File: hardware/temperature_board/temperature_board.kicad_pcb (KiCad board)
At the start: 2 copper layers, 95 x 20 mm, 13 parts, among them J1 RJ45, U1 TSIC50XF, U2 ST485, m3_loch VAL**

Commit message: checking
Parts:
- removed the m3_loch at (230.0, 150.0)
- removed the m3_loch at (200.0, 140.0)
- added m3_loch: VAL**, m3_loch, F.Cu at (134.0, 102.0)
- added m3_loch: VAL**, m3_loch, F.Cu at (104.0, 92.0)
- moved C1 107.3 mm to (106.0, 102.0)
- moved C2 107.3 mm to (115.0, 102.0)
- moved C3 107.3 mm to (115.0, 92.0)
- moved C4 107.3 mm to (125.0, 99.0)
- moved J1 107.3 mm to (144.5, 97.0)
- moved R1 107.3 mm to (110.0, 102.0)
- moved R2 107.3 mm to (122.0, 101.0)
- moved R3 107.3 mm to (122.0, 93.0)
- moved R4 107.3 mm to (125.0, 95.0)
- moved U1 107.3 mm to (73.0, 97.0)
- moved U2 107.3 mm to (117.0, 97.0)
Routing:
- net GND: track 142.1 -> 143.1 mm
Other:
- net class uc added: clearance 0.254, trace_width 0.4, via_dia 1.2, via_drill 0.6

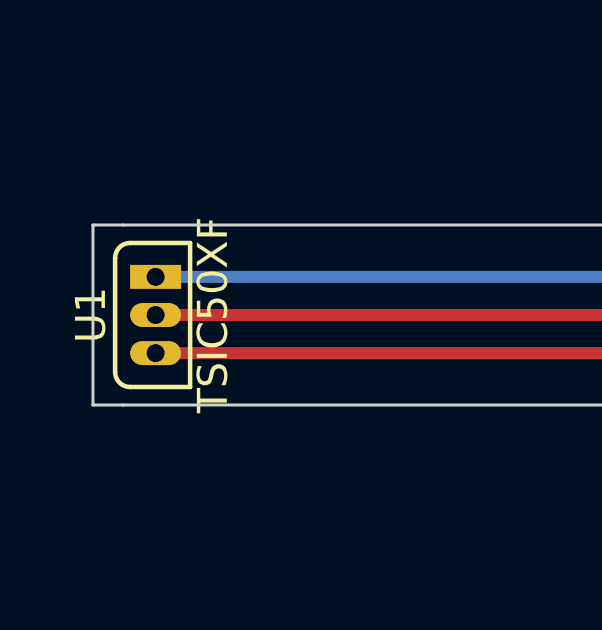
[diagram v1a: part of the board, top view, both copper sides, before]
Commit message: change sensor modules
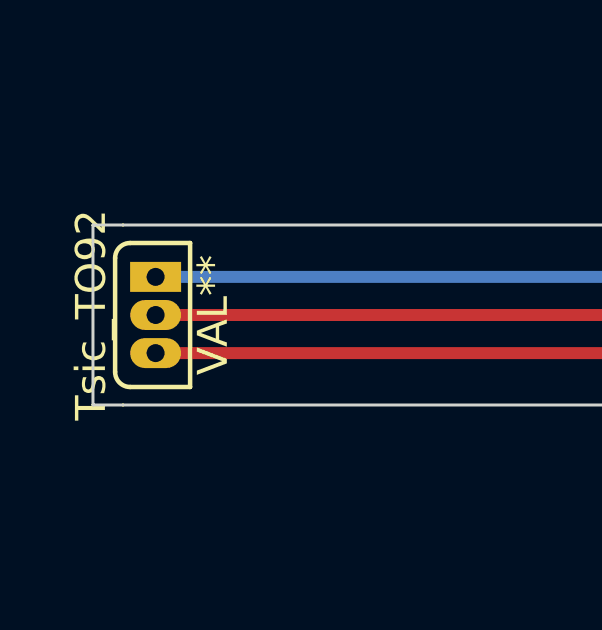
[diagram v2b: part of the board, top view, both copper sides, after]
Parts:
- removed U1: TSIC50XF, Tsic_TO92
- added Tsic_TO92: VAL**, Tsic_TO92, F.Cu at (73.0, 97.0)
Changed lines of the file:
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@@
 (kicad_pcb (version 3) (host pcbnew "(2013-may-18)-stable")
   (general
-    (links 27)
+    (links 24)
     (no_connects 0)
     (area 53.714288 80.150001 208.999999 118.7)
@@
     (add_net N-000007)
   )
+  (module Tsic_TO92 (layer F.Cu)
+    (at 73 97 270)
+    (fp_text reference Tsic_TO92 (at 0 4.064 270) (layer F.SilkS)
+      (effects (font (size 1 1) (thickness 0.15)))
+    )
+    (fp_text value VAL** (at 0 0 270) (layer F.SilkS)
+      (effects (font (size 1 1) (thickness 0.15)))
+    )
+    (fp_arc (start 1.9 2.762) (end 2.4 2.762) (angle 90) (layer F.SilkS) (width 0.15))
+    (fp_arc (start -1.9 2.762) (end -1.9 3.262) (angle 90) (layer F.SilkS) (width 0.15))
+    (fp_line (start -2.4 0.762) (end 2.4 0.762) (layer F.SilkS) (width 0.15))
+    (fp_line (start 2.4 0.762) (end 2.4 2.762) (layer F.SilkS) (width 0.15))
+    (fp_line (start 1.9 3.262) (end -1.9 3.262) (layer F.SilkS) (width 0.15))
+    (fp_line (start -2.4 2.762) (end -2.4 0.762) (layer F.SilkS) (width 0.15))
+    (pad 2 thru_hole oval (at 0 1.912 270) (size 1 1.7) (drill 0.6)
+      (layers *.Cu *.Mask F.SilkS)
+    )
+    (pad 1 thru_hole trapezoid (at -1.27 1.912 270) (size 1 1.7) (drill 0.6)
+      (layers *.Cu *.Mask F.SilkS)
+    )
+    (pad 3 thru_hole oval (at 1.27 1.912 270) (size 1 1.7) (drill 0.6)
+      (layers *.Cu *.Mask F.SilkS)
+    )
+  )
   (module RJ45_8P8_simple (layer F.Cu)
     (at 144.5 97 270)
@@
       (scale (xyz 0.4 0.4 0.4))
       (rotate (xyz 0 0 0))
-    )
-  )
-  (module Tsic_TO92 (layer F.Cu)
-    (at 73 97 270)
-    (fp_text reference U1 (at 0 4.064 270) (layer F.SilkS)
-      (effects (font (size 1 1) (thickness 0.15)))
-    )
-    (fp_text value TSIC50XF (at 0 0 270) (layer F.SilkS)
-      (effects (font (size 1 1) (thickness 0.15)))
-    )
-    (fp_arc (start 1.9 2.762) (end 2.4 2.762) (angle 90) (layer F.SilkS) (width 0.15))
-    (fp_arc (start -1.9 2.762) (end -1.9 3.262) (angle 90) (layer F.SilkS) (width 0.15))
-    (fp_line (start -2.4 0.762) (end 2.4 0.762) (layer F.SilkS) (width 0.15))
-    (fp_line (start 2.4 0.762) (end 2.4 2.762) (layer F.SilkS) (width 0.15))
-    (fp_line (start 1.9 3.262) (end -1.9 3.262) (layer F.SilkS) (width 0.15))
-    (fp_line (start -2.4 2.762) (end -2.4 0.762) (layer F.SilkS) (width 0.15))
-    (pad 2 thru_hole oval (at 0 1.912 270) (size 0.8 1.7) (drill 0.6)
-      (layers *.Cu *.Mask F.SilkS)
-      (net 6 N-000007)
-    )
-    (pad 1 thru_hole trapezoid (at -1.27 1.912 270) (size 0.8 1.7) (drill 0.6)
-      (layers *.Cu *.Mask F.SilkS)
-      (net 3 GND)
-    )
-    (pad 3 thru_hole oval (at 1.27 1.912 270) (size 0.8 1.7) (drill 0.6)
-      (layers *.Cu *.Mask F.SilkS)
-      (net 4 N-0000010)
     )
   )
@@
   (segment (start 125 94.055) (end 122.11 94.055) (width 0.7) (layer F.Cu) (net 2))
   (segment (start 122.11 94.055) (end 122 93.945) (width 0.7) (layer F.Cu) (net 2))
-  (segment (start 71.088 95.73) (end 99.73 95.73) (width 0.4) (layer B.Cu) (net 3))
+  (segment (start 71.088 95.73) (end 99.73 95.73) (width 0.4) (layer B.Cu) (net 3) (status 10))
   (segment (start 118.3 90.5) (end 119.8 92) (width 0.4) (layer B.Cu) (net 3))
   (segment (start 113.5 90.5) (end 118.3 90.5) (width 0.4) (layer B.Cu) (net 3))
@@
   (segment (start 117 102) (end 115.945 102) (width 0.7) (layer F.Cu) (net 3))
   (segment (start 118.2 100.8) (end 117 102) (width 0.7) (layer F.Cu) (net 3))
-  (segment (start 71.088 98.27) (end 98.27 98.27) (width 0.4) (layer F.Cu) (net 4))
+  (segment (start 71.088 98.27) (end 98.27 98.27) (width 0.4) (layer F.Cu) (net 4) (status 10))
   (segment (start 107.555 100.5) (end 109.055 102) (width 0.4) (layer F.Cu) (net 4))
   (segment (start 100.5 100.5) (end 107.555 100.5) (width 0.4) (layer F.Cu) (net 4))
@@
   (segment (start 106.945 102) (end 109.055 102) (width 0.7) (layer F.Cu) (net 4))
   (segment (start 125 95.945) (end 125 98.055) (width 0.7) (layer F.Cu) (net 5))
-  (segment (start 71.088 97) (end 99 97) (width 0.4) (layer F.Cu) (net 6))
+  (segment (start 71.088 97) (end 99 97) (width 0.4) (layer F.Cu) (net 6) (status 10))
   (segment (start 100.902 98.902) (end 111.9 98.902) (width 0.4) (layer F.Cu) (net 6))
   (segment (start 99 97) (end 100.902 98.902) (width 0.4) (layer F.Cu) (net 6))

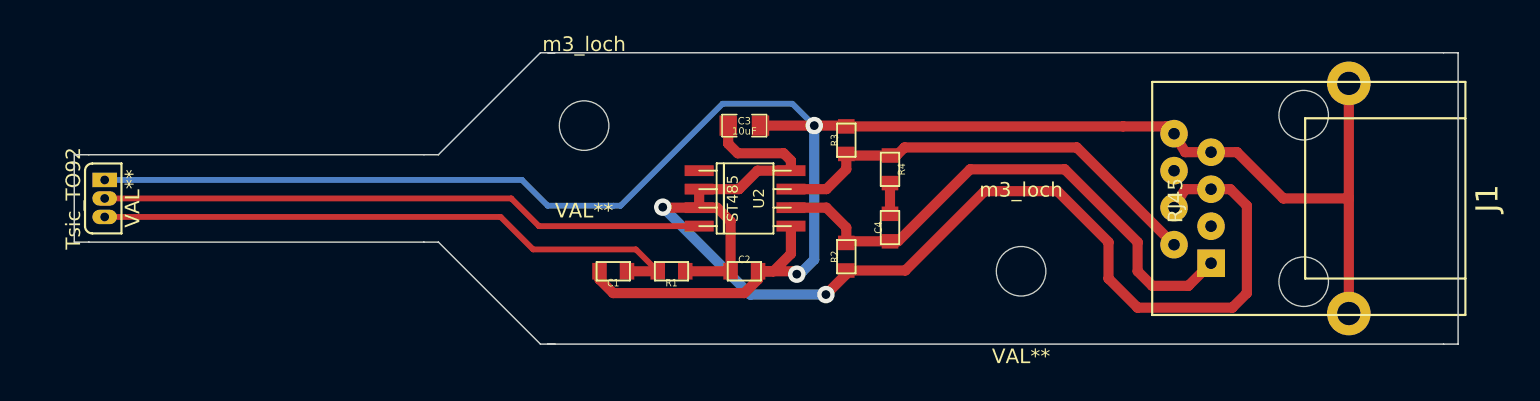
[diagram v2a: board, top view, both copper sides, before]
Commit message: change humidity
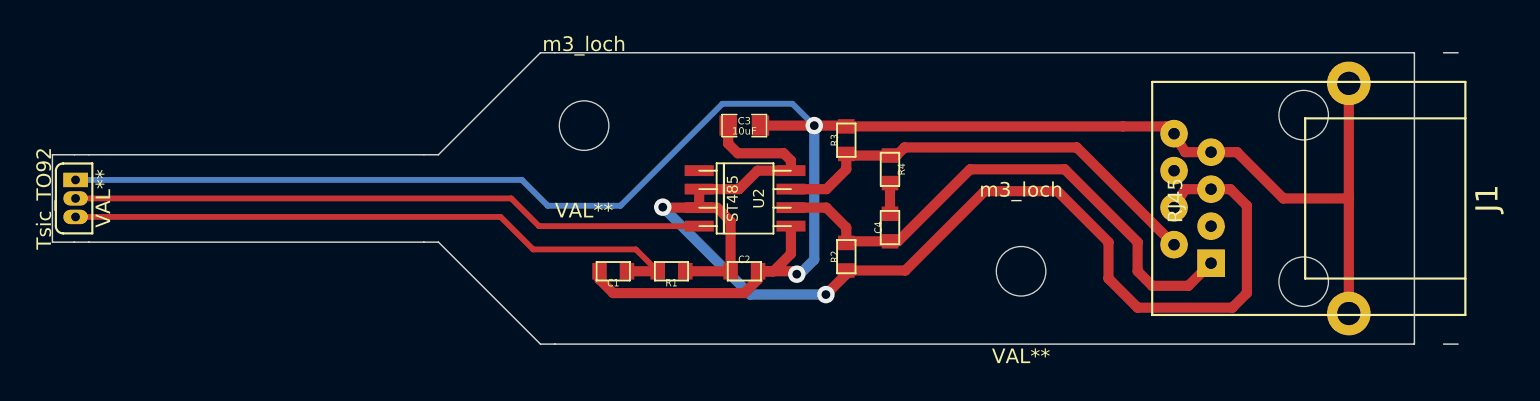
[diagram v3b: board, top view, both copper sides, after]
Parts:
- moved Tsic_TO92 2.00 mm to (71.0, 97.0)
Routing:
- net N-000007: track 41.6 -> 43.6 mm
- net N-0000010: track 41.6 -> 43.6 mm
- net GND: track 143.1 -> 145.1 mm
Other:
- board size 95 x 20 mm -> 96.5 x 20 mm
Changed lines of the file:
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@@
     (area 53.714288 80.150001 208.999999 118.7)
     (thickness 1.6)
-    (drawings 23)
+    (drawings 24)
     (tracks 102)
     (zones 0)
@@
   )
   (module Tsic_TO92 (layer F.Cu)
-    (at 73 97 270)
+    (at 71 97 270)
     (fp_text reference Tsic_TO92 (at 0 4.064 270) (layer F.SilkS)
       (effects (font (size 1 1) (thickness 0.15)))
@@
     )
   )
-  (dimension 27 (width 0.3) (layer Cmts.User)
-    (gr_text "27.000 mm" (at 131.5 111.349999) (layer Cmts.User)
+  (gr_line (start 67.5 100) (end 69 100) (angle 90) (layer Edge.Cuts) (width 0.1))
+  (gr_line (start 67.5 94) (end 67.5 100) (angle 90) (layer Edge.Cuts) (width 0.1))
+  (gr_line (start 69 94) (end 67.5 94) (angle 90) (layer Edge.Cuts) (width 0.1))
+  (dimension 92 (width 0.3) (layer Cmts.User)
+    (gr_text "92.000 mm" (at 115 116.849999) (layer Cmts.User)
       (effects (font (size 1.5 1.5) (thickness 0.3)))
     )
-    (feature1 (pts (xy 145 98) (xy 145 112.699999)))
-    (feature2 (pts (xy 118 98) (xy 118 112.699999)))
-    (crossbar (pts (xy 118 109.999999) (xy 145 109.999999)))
-    (arrow1a (pts (xy 145 109.999999) (xy 143.873497 110.586419)))
-    (arrow1b (pts (xy 145 109.999999) (xy 143.873497 109.413579)))
-    (arrow2a (pts (xy 118 109.999999) (xy 119.126503 110.586419)))
-    (arrow2b (pts (xy 118 109.999999) (xy 119.126503 109.413579)))
-  )
+    (feature1 (pts (xy 69 109) (xy 69 118.199999)))
+    (feature2 (pts (xy 161 109) (xy 161 118.199999)))
+    (crossbar (pts (xy 161 115.499999) (xy 69 115.499999)))
+    (arrow1a (pts (xy 69 115.499999) (xy 70.126503 114.913579)))
+    (arrow1b (pts (xy 69 115.499999) (xy 70.126503 116.086419)))
+    (arrow2a (pts (xy 161 115.499999) (xy 159.873497 114.913579)))
+    (arrow2b (pts (xy 161 115.499999) (xy 159.873497 116.086419)))
+  )
+  (gr_line (start 161 107) (end 102 107) (angle 90) (layer Edge.Cuts) (width 0.1))
+  (gr_line (start 161 87) (end 161 107) (angle 90) (layer Edge.Cuts) (width 0.1))
+  (gr_line (start 102 87) (end 161 87) (angle 90) (layer Edge.Cuts) (width 0.1))
   (gr_line (start 93 100) (end 94 100) (angle 90) (layer Edge.Cuts) (width 0.1))
   (gr_line (start 94 94) (end 93 94) (angle 90) (layer Edge.Cuts) (width 0.1))
@@
   (gr_line (start 94 94) (end 101 87) (angle 90) (layer Edge.Cuts) (width 0.1))
   (gr_line (start 164 107) (end 163 107) (angle 90) (layer Edge.Cuts) (width 0.1))
-  (gr_line (start 164 87) (end 164 107) (angle 90) (layer Edge.Cuts) (width 0.1))
   (gr_line (start 163 87) (end 164 87) (angle 90) (layer Edge.Cuts) (width 0.1))
-  (dimension 95 (width 0.3) (layer Cmts.User)
-    (gr_text "95.000 mm" (at 116.5 117.349999) (layer Cmts.User)
-      (effects (font (size 1.5 1.5) (thickness 0.3)))
-    )
-    (feature1 (pts (xy 69 107) (xy 69 118.699999)))
-    (feature2 (pts (xy 164 107) (xy 164 118.699999)))
-    (crossbar (pts (xy 164 115.999999) (xy 69 115.999999)))
-    (arrow1a (pts (xy 69 115.999999) (xy 70.126503 115.413579)))
-    (arrow1b (pts (xy 69 115.999999) (xy 70.126503 116.586419)))
-    (arrow2a (pts (xy 164 115.999999) (xy 162.873497 115.413579)))
-    (arrow2b (pts (xy 164 115.999999) (xy 162.873497 116.586419)))
-  )
   (dimension 6 (width 0.3) (layer Cmts.User)
     (gr_text "6.000 mm" (at 59.650001 97 270) (layer Cmts.User)
@@
   )
   (gr_line (start 69 94) (end 70 94) (angle 90) (layer Edge.Cuts) (width 0.1))
-  (gr_line (start 69 100) (end 69 94) (angle 90) (layer Edge.Cuts) (width 0.1))
   (gr_line (start 70 100) (end 69 100) (angle 90) (layer Edge.Cuts) (width 0.1))
   (dimension 20 (width 0.3) (layer Cmts.User)
@@
     (arrow2b (pts (xy 200.999999 87.000003) (xy 201.586419 88.126506)))
   )
-  (gr_line (start 101.5 87) (end 163 87) (angle 90) (layer Edge.Cuts) (width 0.1))
-  (gr_line (start 101.5 107) (end 163 107) (angle 90) (layer Edge.Cuts) (width 0.1))
   (dimension 30 (width 0.3) (layer Cmts.User)
     (gr_text "30.000 mm" (at 119 81.650001) (layer Cmts.User)
@@
   (segment (start 125 94.055) (end 122.11 94.055) (width 0.7) (layer F.Cu) (net 2))
   (segment (start 122.11 94.055) (end 122 93.945) (width 0.7) (layer F.Cu) (net 2))
-  (segment (start 71.088 95.73) (end 99.73 95.73) (width 0.4) (layer B.Cu) (net 3) (status 10))
+  (segment (start 69.088 95.73) (end 99.73 95.73) (width 0.4) (layer B.Cu) (net 3) (status 10))
   (segment (start 118.3 90.5) (end 119.8 92) (width 0.4) (layer B.Cu) (net 3))
   (segment (start 113.5 90.5) (end 118.3 90.5) (width 0.4) (layer B.Cu) (net 3))
@@
   (segment (start 117 102) (end 115.945 102) (width 0.7) (layer F.Cu) (net 3))
   (segment (start 118.2 100.8) (end 117 102) (width 0.7) (layer F.Cu) (net 3))
-  (segment (start 71.088 98.27) (end 98.27 98.27) (width 0.4) (layer F.Cu) (net 4) (status 10))
+  (segment (start 69.088 98.27) (end 98.27 98.27) (width 0.4) (layer F.Cu) (net 4) (status 10))
   (segment (start 107.555 100.5) (end 109.055 102) (width 0.4) (layer F.Cu) (net 4))
   (segment (start 100.5 100.5) (end 107.555 100.5) (width 0.4) (layer F.Cu) (net 4))
@@
   (segment (start 106.945 102) (end 109.055 102) (width 0.7) (layer F.Cu) (net 4))
   (segment (start 125 95.945) (end 125 98.055) (width 0.7) (layer F.Cu) (net 5))
-  (segment (start 71.088 97) (end 99 97) (width 0.4) (layer F.Cu) (net 6) (status 10))
+  (segment (start 69.088 97) (end 99 97) (width 0.4) (layer F.Cu) (net 6) (status 10))
   (segment (start 100.902 98.902) (end 111.9 98.902) (width 0.4) (layer F.Cu) (net 6))
   (segment (start 99 97) (end 100.902 98.902) (width 0.4) (layer F.Cu) (net 6))

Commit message: optimal temperature pcb
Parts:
- removed Tsic_TO92: VAL**, Tsic_TO92
- added U1: TSIC50XF, Tsic_TO92, F.Cu at (87.5, 97.0)
- moved C2 17.3 mm to (127.2, 89.8), turned to 90 degrees
- moved C3 15.9 mm to (130.8, 89.8), turned to 90 degrees
- moved m3_loch 15.8 mm to (119.8, 92.0)
- moved R2 13.9 mm to (134.2, 94.5)
- moved C4 13.5 mm to (138.0, 95.2)
- moved R4 13.5 mm to (138.0, 91.2)
- moved R3 12.7 mm to (134.2, 89.5)
- moved C1 12.7 mm to (118.5, 104.2)
- moved R1 12.7 mm to (122.5, 104.2)
- moved U2 11.2 mm to (128.2, 97.0), turned to 315 degrees
- moved m3_loch 1.75 mm to (135.8, 102.0)
- moved J1 0.50 mm to (144.0, 97.0)
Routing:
- net VCC: track 89.5 -> 57.7 mm, vias 2 -> 3
- net GND: track 145.1 -> 122.5 mm, vias 2 -> 1
- net /za: track 37.7 -> 24.1 mm
- net /zb: track 31.0 -> 24.9 mm
- net N-0000010: track 43.6 -> 39.5 mm
- net N-000007: track 43.6 -> 45.5 mm
- added copper zone on B.Cu, net GND
- added copper zone on F.Cu, net GND
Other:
- board size 96.5 x 20 mm -> 76 x 20 mm
